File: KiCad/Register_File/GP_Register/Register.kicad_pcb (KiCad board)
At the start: 2 copper layers, 100 x 100 mm, 59 parts, among them J1 Conn_01x02_Pin, J2 Conn_01x02_Pin, J3 Conn_01x02_Pin, J4 Conn_01x08_Pin, J5 Conn_01x08_Pin, J6 Conn_01x04_Pin, J7 Conn_01x04_Pin, J8 Conn_01x04_Pin, J9 Conn_01x04_Pin, SW1 SW_SPDT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

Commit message: finished registier file boards
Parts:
- removed SW1: SW_SPDT, Button_Switch_THT:SW_Slide_SPDT_Angled_CK_OS102011MA1Q
- added C8: 10n, Capacitor_THT:C_Disc_D3.8mm_W2.6mm_P2.50mm, F.Cu at (157.2, 70.8)
- added C9: 10n, Capacitor_THT:C_Disc_D3.8mm_W2.6mm_P2.50mm, F.Cu at (118.2, 68.0)
- added SW2: SW_SPDT, Button_Switch_THT:SW_Slide_SPDT_Angled_CK_OS102011MA1Q, F.Cu at (117.5, 54.0)
- added U7: 74LS245, Package_DIP:DIP-20_W7.62mm_Socket_LongPads, F.Cu at (121.8, 78.5)
- added U8: 74LS245, Package_DIP:DIP-20_W7.62mm_Socket_LongPads, F.Cu at (160.2, 78.5)
- R10, R12, R13, R14, R15, R16, R17, R18, R2, R3, R4, R5, R6, R7, R8, R9: footprint Resistor_THT:R_Axial_DIN0204_L3.6mm_D1.6mm_P7.62mm_Horizontal -> Resistor_SMD:R_1206_3216Metric_Pad1.30x1.75mm_HandSolder
- moved C2 11.9 mm to (149.0, 86.5), turned to 90 degrees
- moved C3 11.9 mm to (170.8, 86.5), turned to 90 degrees
- moved C4 11.9 mm to (196.6, 86.6), turned to 90 degrees
- moved C1 11.9 mm to (128.8, 86.5), turned to 90 degrees
- moved C6 11.5 mm to (111.8, 132.3)
- moved J6 6.90 mm to (114.0, 91.7)
- moved J9 6.90 mm to (182.0, 91.7)
- moved U1 6.90 mm to (117.8, 86.6)
- moved J7 6.90 mm to (134.5, 91.6)
- moved J8 6.90 mm to (156.0, 91.6)
- moved U2 6.90 mm to (138.1, 86.5)
- moved U4 6.90 mm to (159.9, 86.5)
- moved U5 6.90 mm to (185.7, 86.6)
- moved R2 6.48 mm to (124.0, 60.5)
- moved R3 6.48 mm to (128.0, 60.5)
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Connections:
- net /DE_B renamed /~{DE}
- net /OE_B renamed /~{OE}
- D1 pad 1: Net-(D1-K) -> GND
- D10 pad 1: Net-(D1-K) -> GND
- D11 pad 1: Net-(D1-K) -> GND
- D12 pad 1: Net-(D1-K) -> GND
- D13 pad 1: Net-(D1-K) -> GND
- D14 pad 1: Net-(D1-K) -> GND
- D15 pad 1: Net-(D1-K) -> GND
- D16 pad 1: Net-(D1-K) -> GND
- D2 pad 1: Net-(D1-K) -> GND
- D3 pad 1: Net-(D1-K) -> GND
- D4 pad 1: Net-(D1-K) -> GND
- D5 pad 1: Net-(D1-K) -> GND
- D6 pad 1: Net-(D1-K) -> GND
- D7 pad 1: Net-(D1-K) -> GND
- D8 pad 1: Net-(D1-K) -> GND
- D9 pad 1: Net-(D1-K) -> GND
- J6 pad 1: /Y0 -> Y0
- J6 pad 2: /Y1 -> Y1
- J6 pad 3: /Y2 -> Y2
- J6 pad 4: /Y3 -> Y3
- J7 pad 1: /Y4 -> Y4
- J7 pad 2: /Y5 -> Y5
- J7 pad 3: /Y6 -> Y6
- J7 pad 4: /Y7 -> Y7
- J8 pad 1: /Y8 -> Y8
- J8 pad 2: /Y9 -> Y9
- J8 pad 3: /Y10 -> Y10
- J8 pad 4: /Y11 -> Y11
- J9 pad 1: /Y12 -> Y12
- J9 pad 2: /Y13 -> Y13
- J9 pad 3: /Y14 -> Y14
- J9 pad 4: /Y15 -> Y15
- R10 pad 1: /Y8 -> LED_8
- R12 pad 1: /Y9 -> LED_9
- R13 pad 1: /Y10 -> LED_10
- R14 pad 1: /Y11 -> LED_11
- R15 pad 1: /Y12 -> LED_12
- R16 pad 1: /Y13 -> LED_13
- R17 pad 1: /Y14 -> LED_14
- R18 pad 1: /Y15 -> LED_15
- R2 pad 1: /Y0 -> LED_0
- R3 pad 1: /Y1 -> LED_1
- R4 pad 1: /Y2 -> LED_2
- R5 pad 1: /Y3 -> LED_3
- R6 pad 1: /Y4 -> LED_4
- R7 pad 1: /Y5 -> LED_5
- R8 pad 1: /Y6 -> LED_6
- R9 pad 1: /Y7 -> LED_7
- U1 pad 3: /Y0 -> Y0
- U1 pad 4: /Y1 -> Y1
- U1 pad 5: /Y2 -> Y2
- U1 pad 6: /Y3 -> Y3
- U2 pad 3: /Y4 -> Y4
- U2 pad 4: /Y5 -> Y5
- U2 pad 5: /Y6 -> Y6
- U2 pad 6: /Y7 -> Y7
- U3 pad 11: /Y7 -> Y7
- U3 pad 12: /Y6 -> Y6
- U3 pad 13: /Y5 -> Y5
- U3 pad 14: /Y4 -> Y4
- U3 pad 15: /Y3 -> Y3
- U3 pad 16: /Y2 -> Y2
- U3 pad 17: /Y1 -> Y1
- U3 pad 18: /Y0 -> Y0
- U4 pad 3: /Y8 -> Y8
- U4 pad 4: /Y9 -> Y9
- U4 pad 5: /Y10 -> Y10
- U4 pad 6: /Y11 -> Y11
- U5 pad 3: /Y12 -> Y12
- U5 pad 4: /Y13 -> Y13
- U5 pad 5: /Y14 -> Y14
- U5 pad 6: /Y15 -> Y15
- U6 pad 11: /Y15 -> Y15
- U6 pad 12: /Y14 -> Y14
- U6 pad 13: /Y13 -> Y13
- U6 pad 14: /Y12 -> Y12
- U6 pad 15: /Y11 -> Y11
- U6 pad 16: /Y10 -> Y10
- U6 pad 17: /Y9 -> Y9
- U6 pad 18: /Y8 -> Y8
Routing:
- net /Y3: track 80.6 -> 0.00 mm
- net /Y2: track 77.4 -> 0.00 mm
- net /Y1: track 74.9 -> 0.00 mm
- net +5V: track 214.5 -> 288.7 mm, vias 2 -> 1
- net /Y12: track 73.7 -> 0.00 mm
- net Net-(D1-K): track 71.5 -> 0.00 mm
- net /Y13: track 71.5 -> 0.00 mm
- net /Y0: track 71.3 -> 0.00 mm
- net Y3: track 0.00 -> 70.3 mm
- net /Y14: track 69.6 -> 0.00 mm
- net /Y8: track 69.0 -> 0.00 mm
- net /Y11: track 68.7 -> 0.00 mm
- net /Y9: track 68.3 -> 0.00 mm
- net /Y15: track 68.1 -> 0.00 mm
- net Y2: track 0.00 -> 67.9 mm
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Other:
- board text added: "30/9/24"
- board text added: "rev 1.1"
- board text removed: "24/9/24"
- board text removed: "5V"
- board text removed: "rev 1.0"

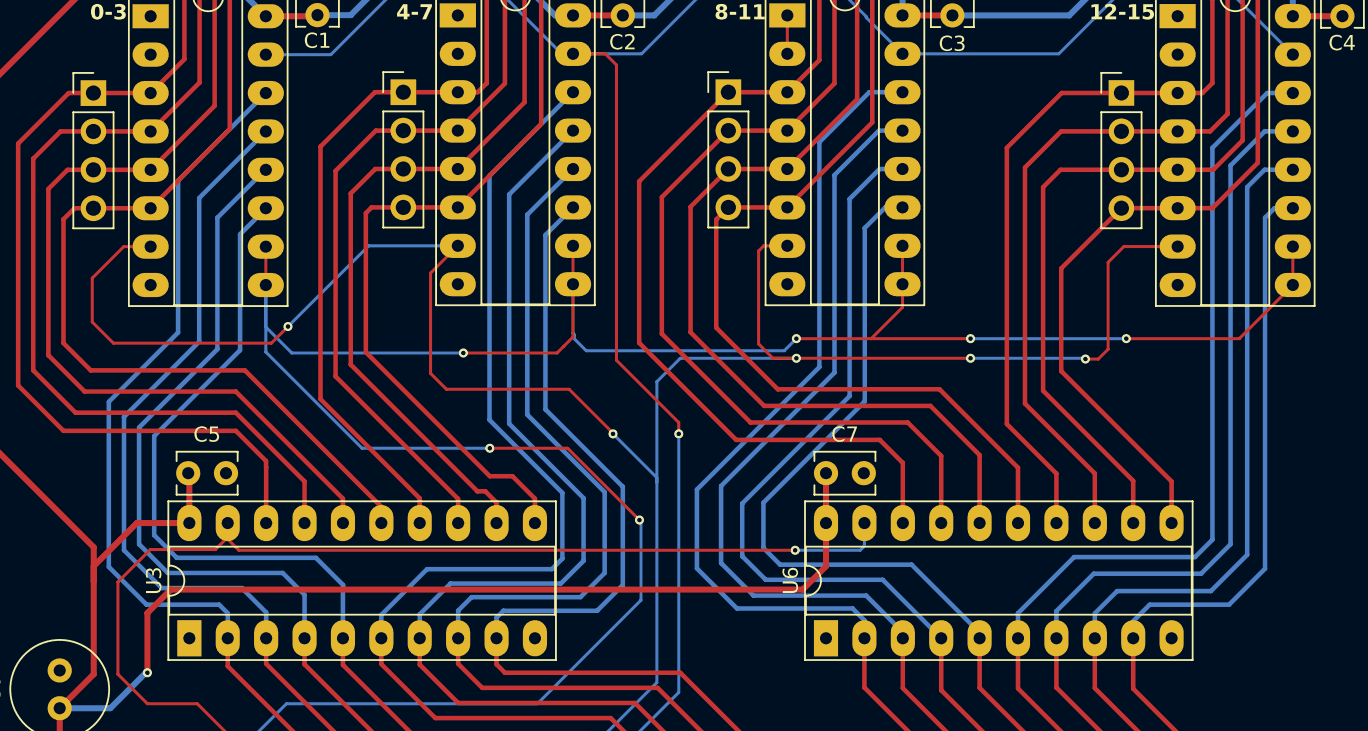
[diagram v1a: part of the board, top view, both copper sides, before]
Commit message: added con_ctrl board mdr_mar
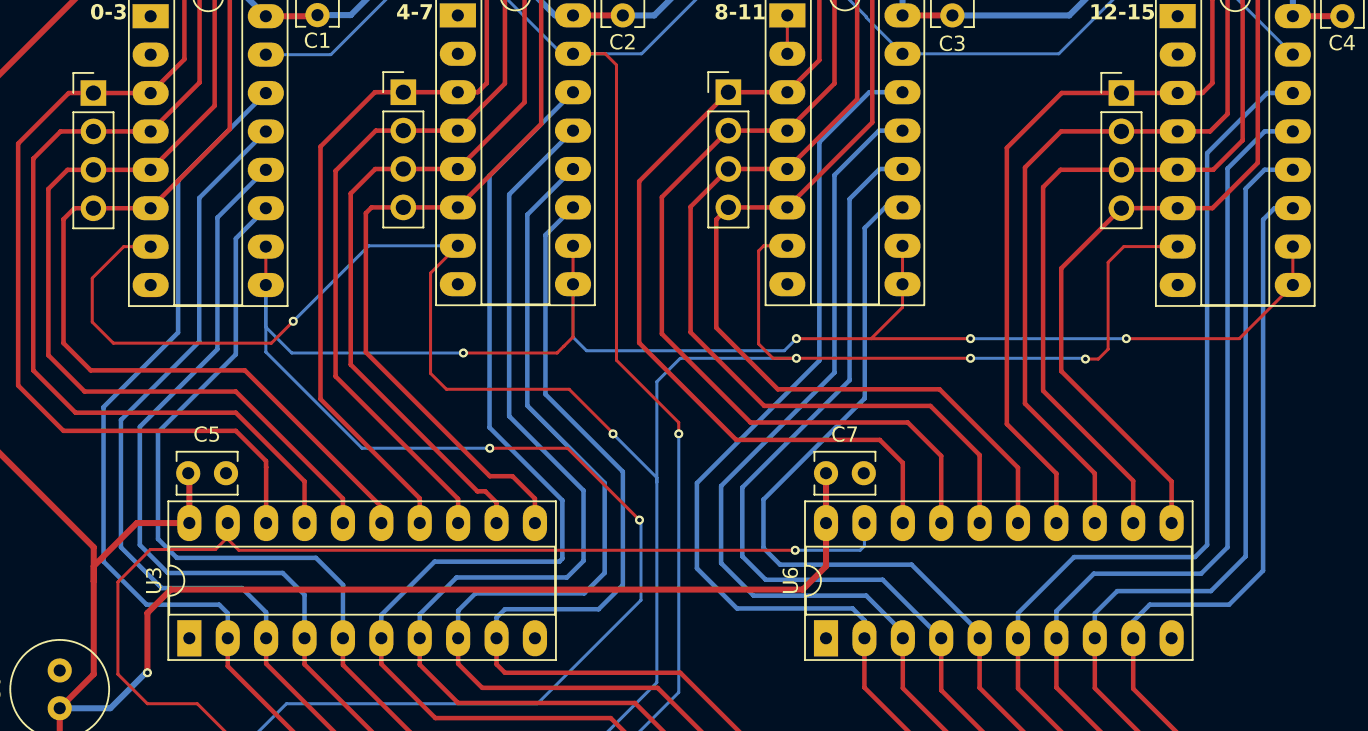
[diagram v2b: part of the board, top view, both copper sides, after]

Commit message: added more boards, added pcb standarts
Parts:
- added J10: Conn_01x02_Pin, elad_jst:JST_XH_S2B-XH-A-1_1x02_P2.50mm_Horizontal_fixed, F.Cu at (121.5, 142.0)
- C1, C2, C3, C4, C5, C7, C8, C9: footprint Capacitor_THT:C_Disc_D3.8mm_W2.6mm_P2.50mm -> Capacitor_SMD:C_1206_3216Metric_Pad1.33x1.80mm_HandSolder
- J1, J2, J3: footprint Connector_JST:JST_XH_S2B-XH-A_1x02_P2.50mm_Horizontal -> elad_jst:JST_XH_S2B-XH-A-1_1x02_P2.50mm_Horizontal_fixed
- moved J2 17.6 mm to (108.0, 131.0), turned to -90 degrees
- moved C6 11.0 mm to (108.0, 122.0), turned to 180 degrees
- moved J3 3.11 mm to (131.0, 142.0)
- moved C8 1.75 mm to (155.5, 70.8)
- moved C1 1.64 mm to (128.7, 88.1), turned to -90 degrees
- moved C4 1.61 mm to (197.0, 88.1), turned to -90 degrees
- moved C3 1.56 mm to (170.8, 88.1), turned to -90 degrees
- moved C7 1.56 mm to (160.9, 116.8), turned to 180 degrees
- moved C2 1.56 mm to (149.5, 88.0), turned to -90 degrees
- moved C5 1.49 mm to (118.8, 116.8), turned to 180 degrees
- moved J1 1.47 mm to (112.0, 142.0)
- moved J4 0.25 mm to (146.0, 142.0)
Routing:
- net +5V: track 288.7 -> 308.8 mm, vias 1 -> 0
- net /~{DE}: track 171.2 -> 190.9 mm
- net GND: track 2.54 -> 12.8 mm, vias 0 -> 12
- net /~{OE}: track 77.0 -> 68.5 mm, vias 1 -> 2
- net /RST: track 149.8 -> 156.9 mm
- net /CLK: track 158.5 -> 162.2 mm
- net Y15: track 62.5 -> 64.0 mm
- net Y4: track 55.9 -> 56.7 mm
- net Y7: track 55.9 -> 55.7 mm, vias 0 -> 1
- net Y6: vias 0 -> 1
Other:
- board text added: "15/10/24"
- board text added: "LSB"
- board text added: "MSB"
- board text added: "VCC"
- board text added: "rev 1.2"
- board text removed: "30/9/24"
- board text removed: "rev 1.1"

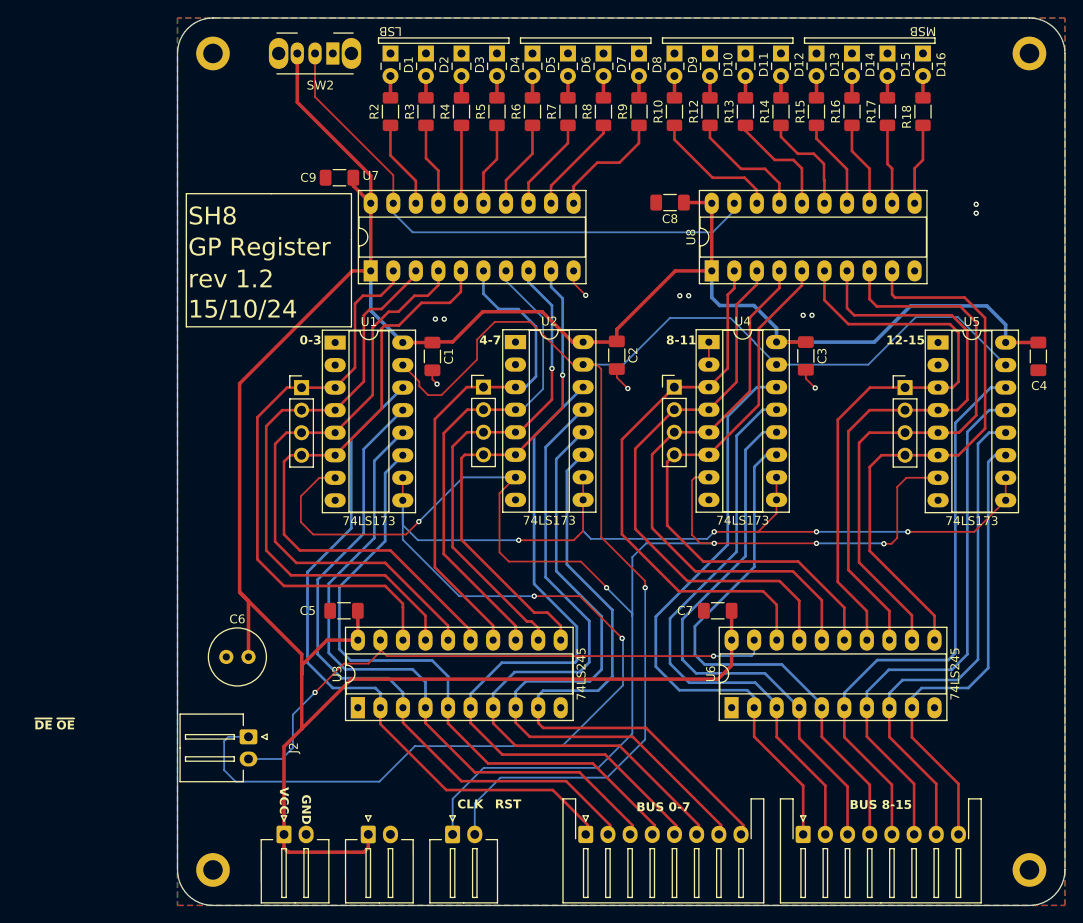
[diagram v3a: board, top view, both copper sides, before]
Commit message: created standarts for PCB's
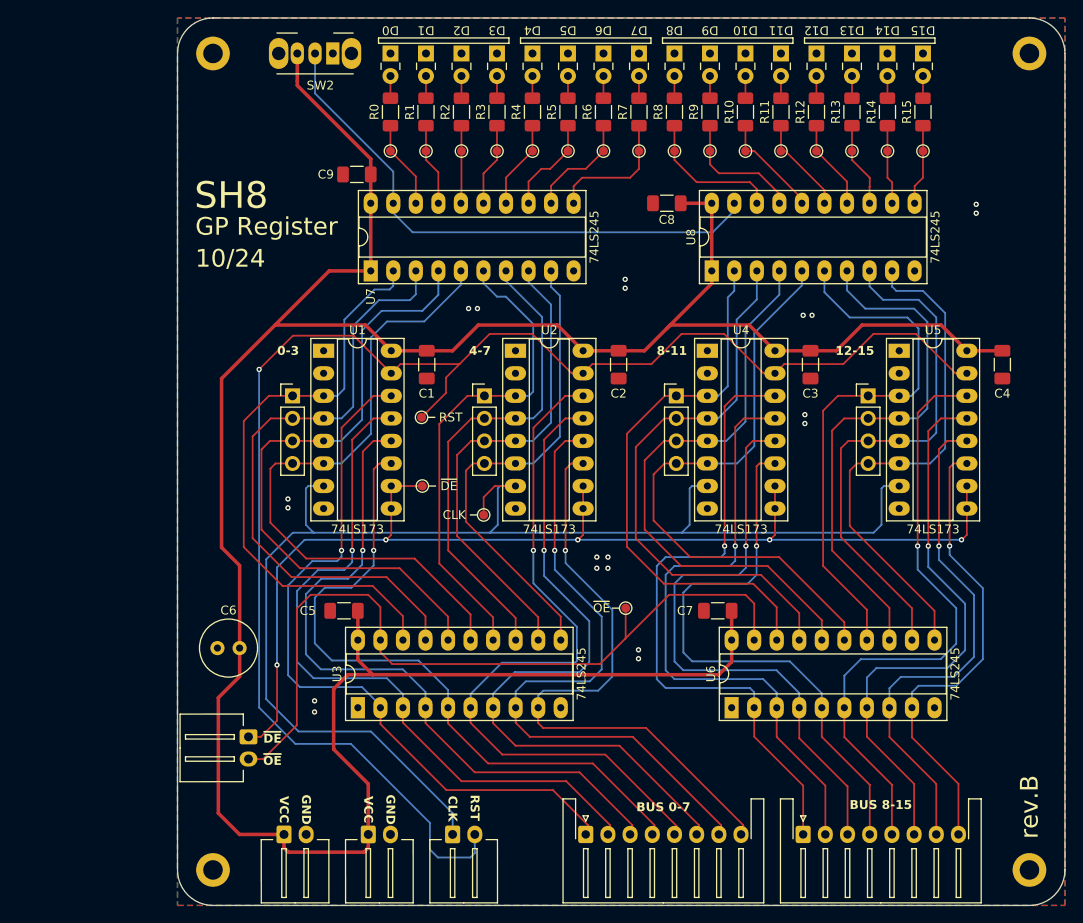
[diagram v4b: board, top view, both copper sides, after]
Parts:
- removed D16: LED, LED_THT:LED_Rectangular_W3.0mm_H2.0mm
- removed R16, R17, R18: 1k, Resistor_SMD:R_1206_3216Metric_Pad1.30x1.75mm_HandSolder
- added D0: LED, LED_THT:LED_Rectangular_W3.0mm_H2.0mm, F.Cu at (124.0, 54.0)
- added R0: 1k, Resistor_SMD:R_1206_3216Metric_Pad1.30x1.75mm_HandSolder, F.Cu at (124.0, 60.6)
- added R1: 1k, Resistor_SMD:R_1206_3216Metric_Pad1.30x1.75mm_HandSolder, F.Cu at (128.0, 60.6)
- added R11: 1k, Resistor_SMD:R_1206_3216Metric_Pad1.30x1.75mm_HandSolder, F.Cu at (168.0, 60.6)
- added TP1: TestPoint, TestPoint:TestPoint_Pad_D1.0mm, F.Cu at (124.0, 65.0)
- added TP10: TestPoint, TestPoint:TestPoint_Pad_D1.0mm, F.Cu at (160.0, 65.0)
- added TP11: TestPoint, TestPoint:TestPoint_Pad_D1.0mm, F.Cu at (164.0, 65.0)
- added TP12: TestPoint, TestPoint:TestPoint_Pad_D1.0mm, F.Cu at (168.0, 65.0)
- added TP13: TestPoint, TestPoint:TestPoint_Pad_D1.0mm, F.Cu at (172.0, 65.0)
- added TP14: TestPoint, TestPoint:TestPoint_Pad_D1.0mm, F.Cu at (176.0, 65.0)
- added TP15: TestPoint, TestPoint:TestPoint_Pad_D1.0mm, F.Cu at (180.0, 65.0)
- added TP16: TestPoint, TestPoint:TestPoint_Pad_D1.0mm, F.Cu at (184.0, 65.0)
- added TP17: TestPoint, TestPoint:TestPoint_Pad_D1.0mm, F.Cu at (150.5, 116.5)
- added TP18: TestPoint, TestPoint:TestPoint_Pad_D1.0mm, F.Cu at (127.6, 102.7)
- added TP19: TestPoint, TestPoint:TestPoint_Pad_D1.0mm, F.Cu at (134.5, 106.0)
- added TP2: TestPoint, TestPoint:TestPoint_Pad_D1.0mm, F.Cu at (128.0, 65.0)
- added TP20: TestPoint, TestPoint:TestPoint_Pad_D1.0mm, F.Cu at (127.5, 95.0)
- added TP3: TestPoint, TestPoint:TestPoint_Pad_D1.0mm, F.Cu at (132.0, 65.0)
- added TP4: TestPoint, TestPoint:TestPoint_Pad_D1.0mm, F.Cu at (136.0, 65.0)
- added TP5: TestPoint, TestPoint:TestPoint_Pad_D1.0mm, F.Cu at (140.0, 65.0)
- added TP6: TestPoint, TestPoint:TestPoint_Pad_D1.0mm, F.Cu at (144.0, 65.0)
- added TP7: TestPoint, TestPoint:TestPoint_Pad_D1.0mm, F.Cu at (148.0, 65.0)
- added TP8: TestPoint, TestPoint:TestPoint_Pad_D1.0mm, F.Cu at (152.0, 65.0)
- added TP9: TestPoint, TestPoint:TestPoint_Pad_D1.0mm, F.Cu at (156.0, 65.0)
- moved R12 12.0 mm to (172.0, 60.6)
- moved R13 12.0 mm to (176.0, 60.6)
- moved R14 12.0 mm to (180.0, 60.6)
- moved R15 12.0 mm to (184.0, 60.6)
- moved R10 8.00 mm to (164.0, 60.6)
- moved R2 8.00 mm to (132.0, 60.6)
- moved R3 8.00 mm to (136.0, 60.6)
- moved R4 8.00 mm to (140.0, 60.6)
- moved R5 8.00 mm to (144.0, 60.6)
- moved R6 8.00 mm to (148.0, 60.6)
- moved R7 8.00 mm to (152.0, 60.6)
- moved R8 8.00 mm to (156.0, 60.6)
- moved R9 8.00 mm to (160.0, 60.6)
- moved U5 4.47 mm to (181.3, 87.5)
- moved J9 4.26 mm to (177.8, 92.6)
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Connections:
- net /CLK renamed CLK
- net /RST renamed RST
- net /~{DE} renamed ~{DE}
- net /~{OE} renamed ~{OE}
- R10 pad 1: LED_8 -> LED_10
- R10 pad 2: Net-(D9-A) -> Net-(D10-A)
- R12 pad 1: LED_9 -> LED_12
- R12 pad 2: Net-(D10-A) -> Net-(D12-A)
- R13 pad 1: LED_10 -> LED_13
- R13 pad 2: Net-(D11-A) -> Net-(D13-A)
- R14 pad 1: LED_11 -> LED_14
- R14 pad 2: Net-(D12-A) -> Net-(D14-A)
- R15 pad 1: LED_12 -> LED_15
- R15 pad 2: Net-(D13-A) -> Net-(D15-A)
- R2 pad 1: LED_0 -> LED_2
- R2 pad 2: Net-(D1-A) -> Net-(D2-A)
- R3 pad 1: LED_1 -> LED_3
- R3 pad 2: Net-(D2-A) -> Net-(D3-A)
- R4 pad 1: LED_2 -> LED_4
- R4 pad 2: Net-(D3-A) -> Net-(D4-A)
- R5 pad 1: LED_3 -> LED_5
- R5 pad 2: Net-(D4-A) -> Net-(D5-A)
- R6 pad 1: LED_4 -> LED_6
- R6 pad 2: Net-(D5-A) -> Net-(D6-A)
- R7 pad 1: LED_5 -> LED_7
- R7 pad 2: Net-(D6-A) -> Net-(D7-A)
- R8 pad 1: LED_6 -> LED_8
- R8 pad 2: Net-(D7-A) -> Net-(D8-A)
- R9 pad 1: LED_7 -> LED_9
- R9 pad 2: Net-(D8-A) -> Net-(D9-A)
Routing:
- net ~{DE}: track 190.9 -> 128.4 mm, vias 6 -> 5
- net ~{OE}: track 68.5 -> 89.8 mm, vias 2 -> 0
- net RST: track 156.9 -> 175.4 mm
- net GND: track 12.8 -> 0.00 mm, vias 12 -> 20
- net CLK: track 162.2 -> 150.1 mm, vias 5 -> 0
- net Y13: track 66.9 -> 60.5 mm
- net Y12: track 67.0 -> 61.1 mm
- net Y14: track 65.9 -> 60.1 mm
- net /B9: track 65.4 -> 71.0 mm, vias 0 -> 1
- net /B10: track 63.0 -> 68.5 mm, vias 0 -> 1
- net /B11: track 60.5 -> 65.9 mm, vias 0 -> 1
- net /B1: track 75.4 -> 80.6 mm, vias 0 -> 1
- net /B8: track 68.9 -> 73.9 mm, vias 0 -> 1
- net Y15: track 64.0 -> 59.1 mm
- net Y2: track 67.9 -> 72.5 mm
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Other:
- board text added: "10/24"
- board text added: "rev.B"
- board text removed: "15/10/24"
- board text removed: "LSB"
- board text removed: "MSB"
- board text removed: "rev 1.2"
